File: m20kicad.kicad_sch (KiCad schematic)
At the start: 16 parts, among them U1 NE555P

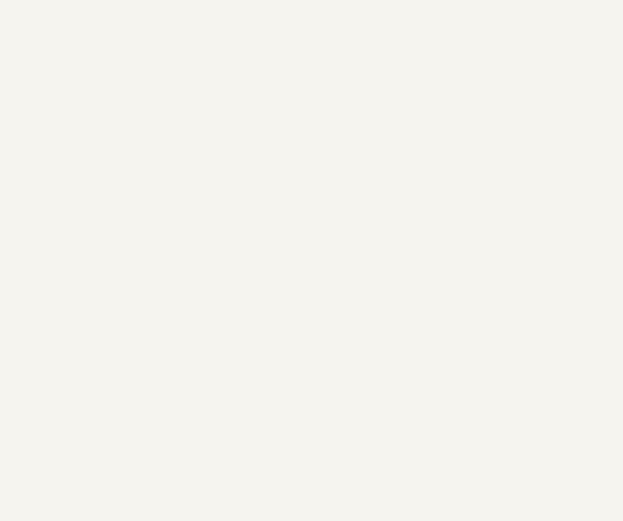
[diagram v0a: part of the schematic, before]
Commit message: adding LPS22 connection
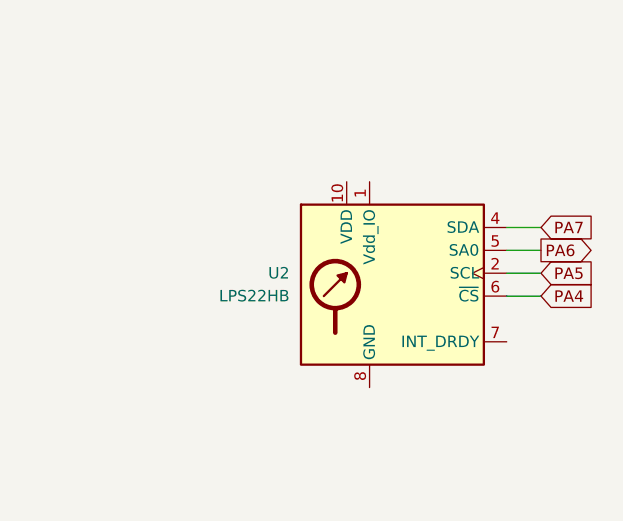
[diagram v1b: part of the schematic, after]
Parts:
- added U2: LPS22HB, Package_LGA:ST_HLGA-10_2x2mm_P0.5mm_LayoutBorder3x2y, symbol Sensor_Pressure:LPS22HB
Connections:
- new net: U2.3 (GND), U2.8 (GND), U2.9 (GND)
- new net PA4: U2.6 (~{CS})
- new net PA5: U2.2 (SCL)
- new net PA6: U2.5 (SA0)
- new net PA7: U2.4 (SDA)
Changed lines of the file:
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@@
+	(wire
+		(pts
+			(xy 226.06 59.69) (xy 229.87 59.69)
+		)
+		(stroke
+			(width 0)
+			(type default)
+		)
+	)
+	(wire
+		(pts
+			(xy 226.06 57.15) (xy 229.87 57.15)
+		)
+		(stroke
+			(width 0)
+			(type default)
+		)
+	)
 	(wire
 		(pts
@@
 	(wire
 		(pts
+			(xy 226.06 62.23) (xy 229.87 62.23)
+		)
+		(stroke
+			(width 0)
+			(type default)
+		)
+	)
+	(wire
+		(pts
 			(xy 90.17 31.75) (xy 92.71 31.75)
 		)
@@
 		(pts
 			(xy 130.81 77.47) (xy 130.81 81.28)
+		)
+		(stroke
+			(width 0)
+			(type default)
+		)
+	)
+	(wire
+		(pts
+			(xy 226.06 64.77) (xy 229.87 64.77)
 		)
 		(stroke
@@
 		)
 	)
+	(global_label "PA5"
+		(shape input)
+		(at 229.87 62.23 0)
+		(fields_autoplaced yes)
+		(effects
+			(font
+				(size 1.27 1.27)
+			)
+			(justify left)
+		)
+		(property "Intersheetrefs" "${INTERSHEET_REFS}"
+			(at 236.4233 62.23 0)
+			(hide yes)
+			(show_name no)
+			(do_not_autoplace no)
+			(effects
+				(font
+					(size 1.27 1.27)
+				)
+				(justify left)
+			)
+		)
+	)
 	(global_label "PB9"
 		(shape input)
@@
 		)
 	)
+	(global_label "PA7"
+		(shape input)
+		(at 229.87 57.15 0)
+		(fields_autoplaced yes)
+		(effects
+			(font
+				(size 1.27 1.27)
+			)
+			(justify left)
+		)
+		(property "Intersheetrefs" "${INTERSHEET_REFS}"
+			(at 236.4233 57.15 0)
+			(hide yes)
+			(show_name no)
+			(do_not_autoplace no)
+			(effects
+				(font
+					(size 1.27 1.27)
+				)
+				(justify left)
+			)
+		)
+	)
 	(global_label "PC2"
 		(shape output)
@@
 		)
 	)
+	(global_label "PA4"
+		(shape input)
+		(at 229.87 64.77 0)
+		(fields_autoplaced yes)
+		(effects
+			(font
+				(size 1.27 1.27)
+			)
+			(justify left)
+		)
+		(property "Intersheetrefs" "${INTERSHEET_REFS}"
+			(at 236.4233 64.77 0)
+			(hide yes)
+			(show_name no)
+			(do_not_autoplace no)
+			(effects
+				(font
+					(size 1.27 1.27)
+				)
+				(justify left)
+			)
+		)
+	)
 	(global_label "PC6"
 		(shape output)
@@
 		(property "Intersheetrefs" "${INTERSHEET_REFS}"
 			(at 80.01 22.4753 90)
+			(hide yes)
+			(show_name no)
+			(do_not_autoplace no)
+			(effects
+				(font
+					(size 1.27 1.27)
+				)
+				(justify left)
+			)
+		)
+	)
+	(global_label "PA6"
+		(shape output)
+		(at 229.87 59.69 0)
+		(fields_autoplaced yes)
+		(effects
+			(font
+				(size 1.27 1.27)
+			)
+			(justify left)
+		)
+		(property "Intersheetrefs" "${INTERSHEET_REFS}"
+			(at 236.4233 59.69 0)
 			(hide yes)
 			(show_name no)
@@
 					(unit 1)
 				)
+			)
+		)
+	)
+	(symbol
+		(lib_id "Sensor_Pressure:LPS22HB")
+		(at 213.36 64.77 0)
+		(unit 1)
+		(body_style 1)
+		(exclude_from_sim no)
+		(in_bom yes)
+		(on_board yes)
+		(in_pos_files yes)
+		(dnp no)
+		(fields_autoplaced yes)
+		(property "Reference" "U2"
+			(at 201.93 62.2299 0)
+			(show_name no)
+			(do_not_autoplace no)
+			(effects
+				(font
+					(size 1.27 1.27)
+				)
+				(justify right)
+			)
+		)
+		(property "Value" "LPS22HB"
+			(at 201.93 64.7699 0)
+			(show_name no)
+			(do_not_autoplace no)
+			(effects
+				(font
+					(size 1.27 1.27)
+				)
+				(justify right)
+			)
+		)
+		(property "Footprint" "Package_LGA:ST_HLGA-10_2x2mm_P0.5mm_LayoutBorder3x2y"
+			(at 214.63 76.2 0)
+			(hide yes)
+			(show_name no)
+			(do_not_autoplace no)
+			(effects
+				(font
+					(size 1.27 1.27)
+				)
+				(justify left)
+			)
+		)
+		(property "Datasheet" "https://www.st.com/resource/en/datasheet/lps22hb.pdf"
+			(at 214.63 78.74 0)
+			(hide yes)
+			(show_name no)
+			(do_not_autoplace no)
+			(effects
+				(font
+					(size 1.27 1.27)
+				)
+				(justify left)
+			)
+		)
+		(property "Description" "MEMS nano pressure sensor, 260-1260 hPa, absolute digital output baromeeter, 24 bit, SPI, I2C, 0.0075 hPa noise rms, ST_HLGA-10L"
+			(at 213.36 64.77 0)
+			(hide yes)
+			(show_name no)
+			(do_not_autoplace no)
+			(effects
+				(font
+					(size 1.27 1.27)
+				)
+			)
+		)
+		(pin "1"
+		)
+		(pin "10"
+		)
+		(pin "7"
+		)
+		(pin "3"
+		)
+		(pin "2"
+		)
+		(pin "6"
+		)
+		(pin "8"
+		)
+		(pin "5"
+		)
+		(pin "4"
+		)
+		(pin "9"
+		)
+		(instances
+			(project "m20kicad"
+				(path "/c087906e-d721-47a2-a6d1-b35611cec6ed"
+					(reference "U2")
+					(unit 1)
+				)

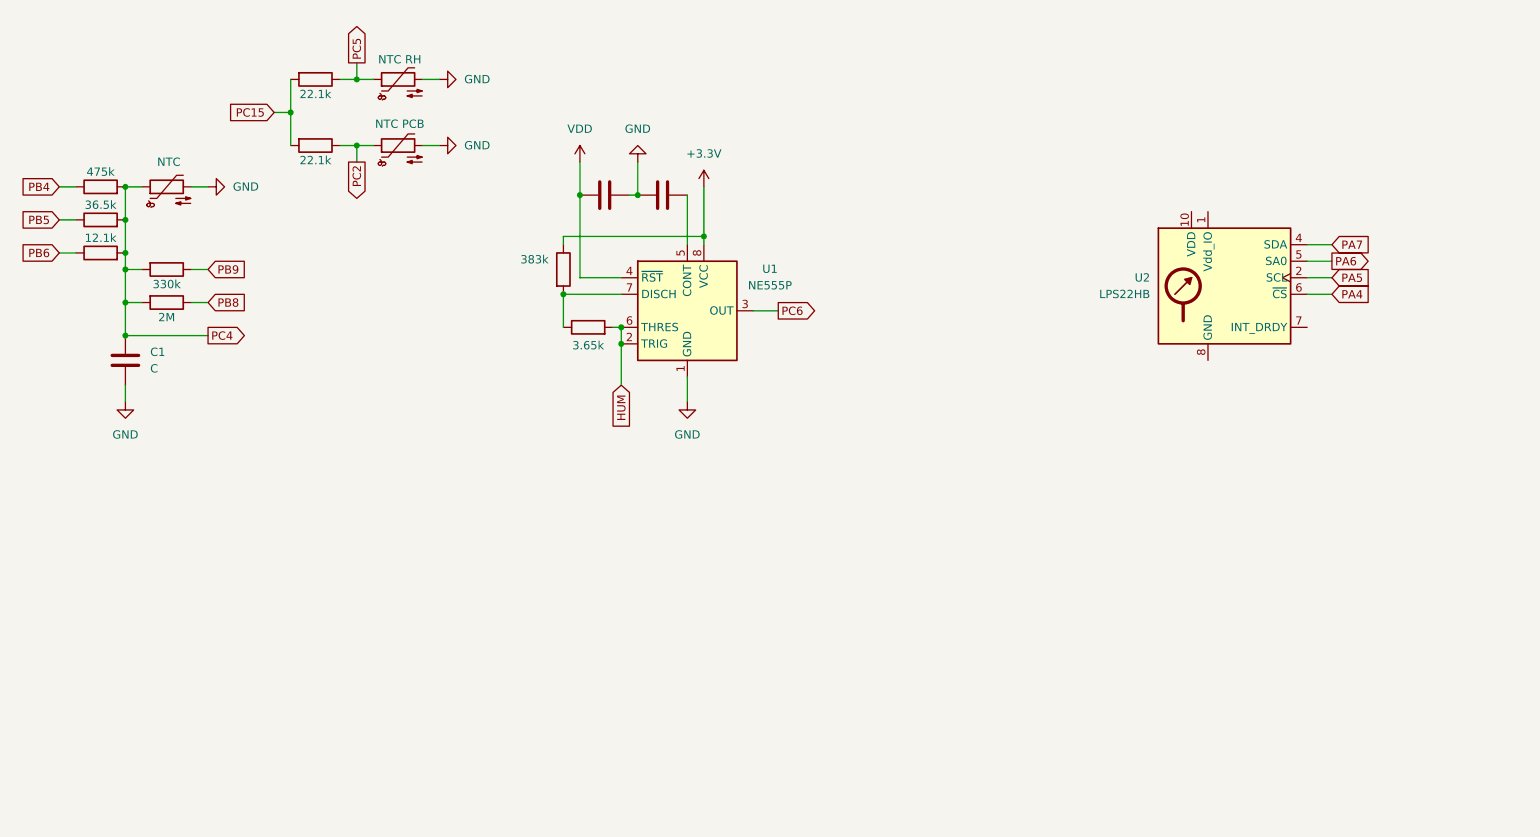
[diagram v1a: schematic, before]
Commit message: adding expansion connector
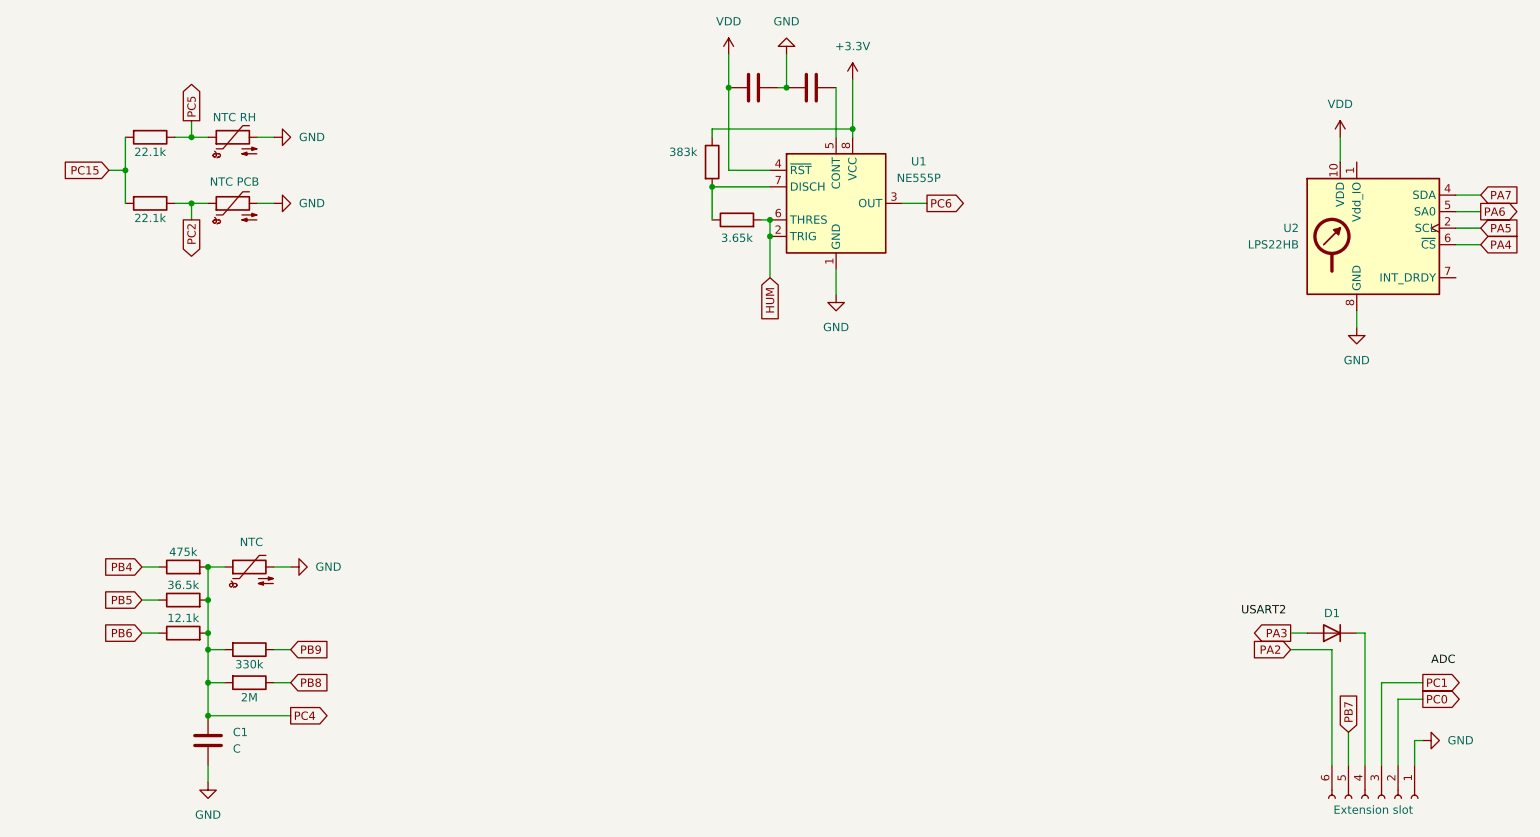
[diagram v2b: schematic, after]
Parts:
- added D1: D, symbol Device:D
- added J1: Extension slot, symbol Connector:Conn_01x06_Socket
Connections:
- net GND: now also U2.3 (GND), U2.8 (GND), U2.9 (GND), J1.1 (Pin_1)
- net VDD: now also U2.10 (VDD)
- new net: D1.1 (K), J1.4 (Pin_4)
- new net PA2: J1.6 (Pin_6)
- new net PA3: D1.2 (A)
- new net PB7: J1.5 (Pin_5)
- new net PC0: J1.2 (Pin_2)
- new net PC1: J1.3 (Pin_3)
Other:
- moved on the sheet: C1, U1, U2
